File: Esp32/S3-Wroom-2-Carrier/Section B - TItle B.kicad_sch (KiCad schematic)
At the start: 2 parts, among them J1 DF9-21S-1V32, J2 DF9-21S-1V32

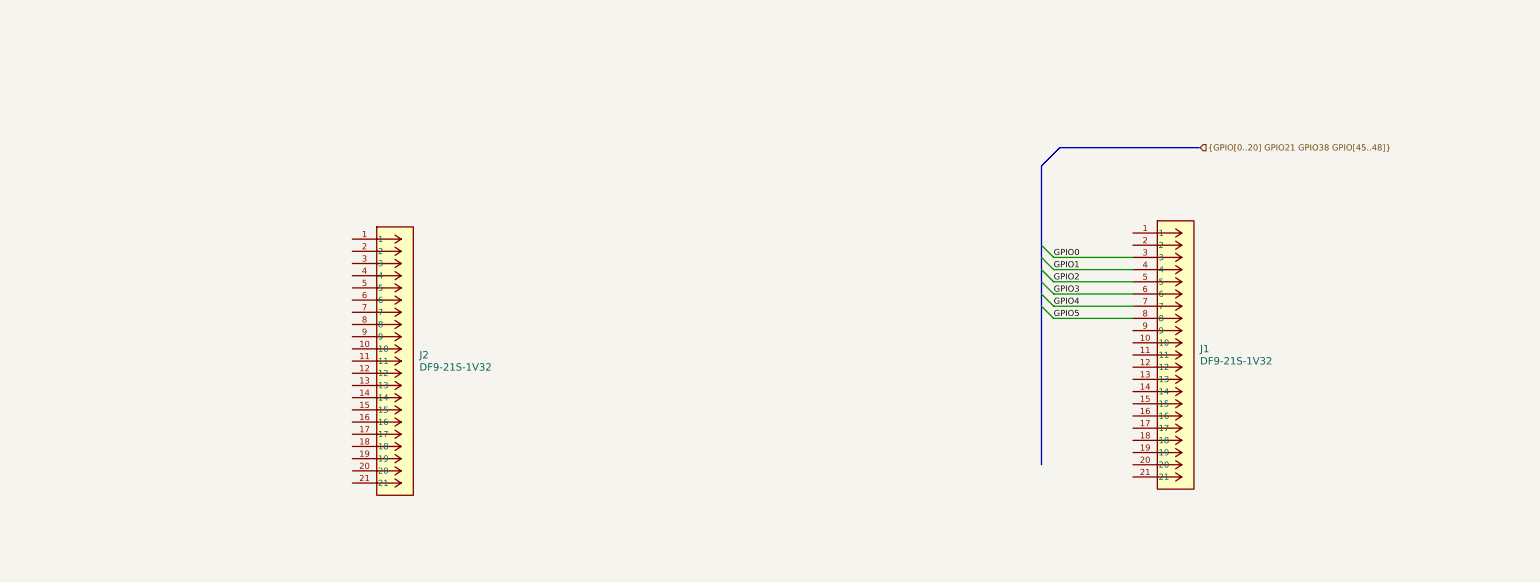
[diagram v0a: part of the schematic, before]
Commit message: Power sheet
Added Esp32 power sheet and rename previous sheets
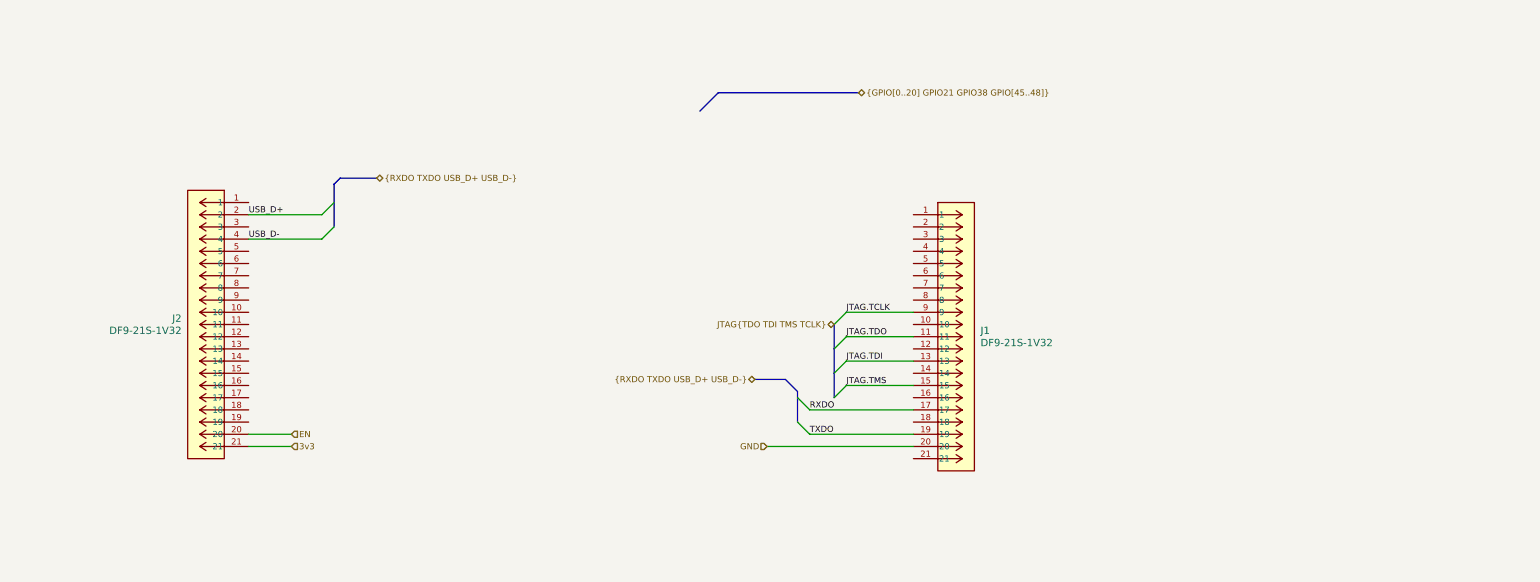
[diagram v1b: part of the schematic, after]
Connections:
- net JTAG.TDO: now reaches J1.11
- net JTAG.TDI: now reaches J1.13
- net JTAG.TMS: now reaches J1.15
- net RXDO: now reaches J1.17
- net TXDO: now reaches J1.19
- net GND: now reaches J1.20
- net JTAG.TCLK: now reaches J1.9
- net USB_D+: now reaches J2.2
- net EN: now reaches J2.20
- net 3v3: now reaches J2.21
- net USB_D-: now reaches J2.4
- net GPIO0: no longer names the net of J1.3
- net GPIO1: no longer names the net of J1.4
- net GPIO2: no longer names the net of J1.5
- net GPIO3: no longer names the net of J1.6
- net GPIO4: no longer names the net of J1.7
- net GPIO5: no longer names the net of J1.8
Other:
- moved on the sheet: J1, J2

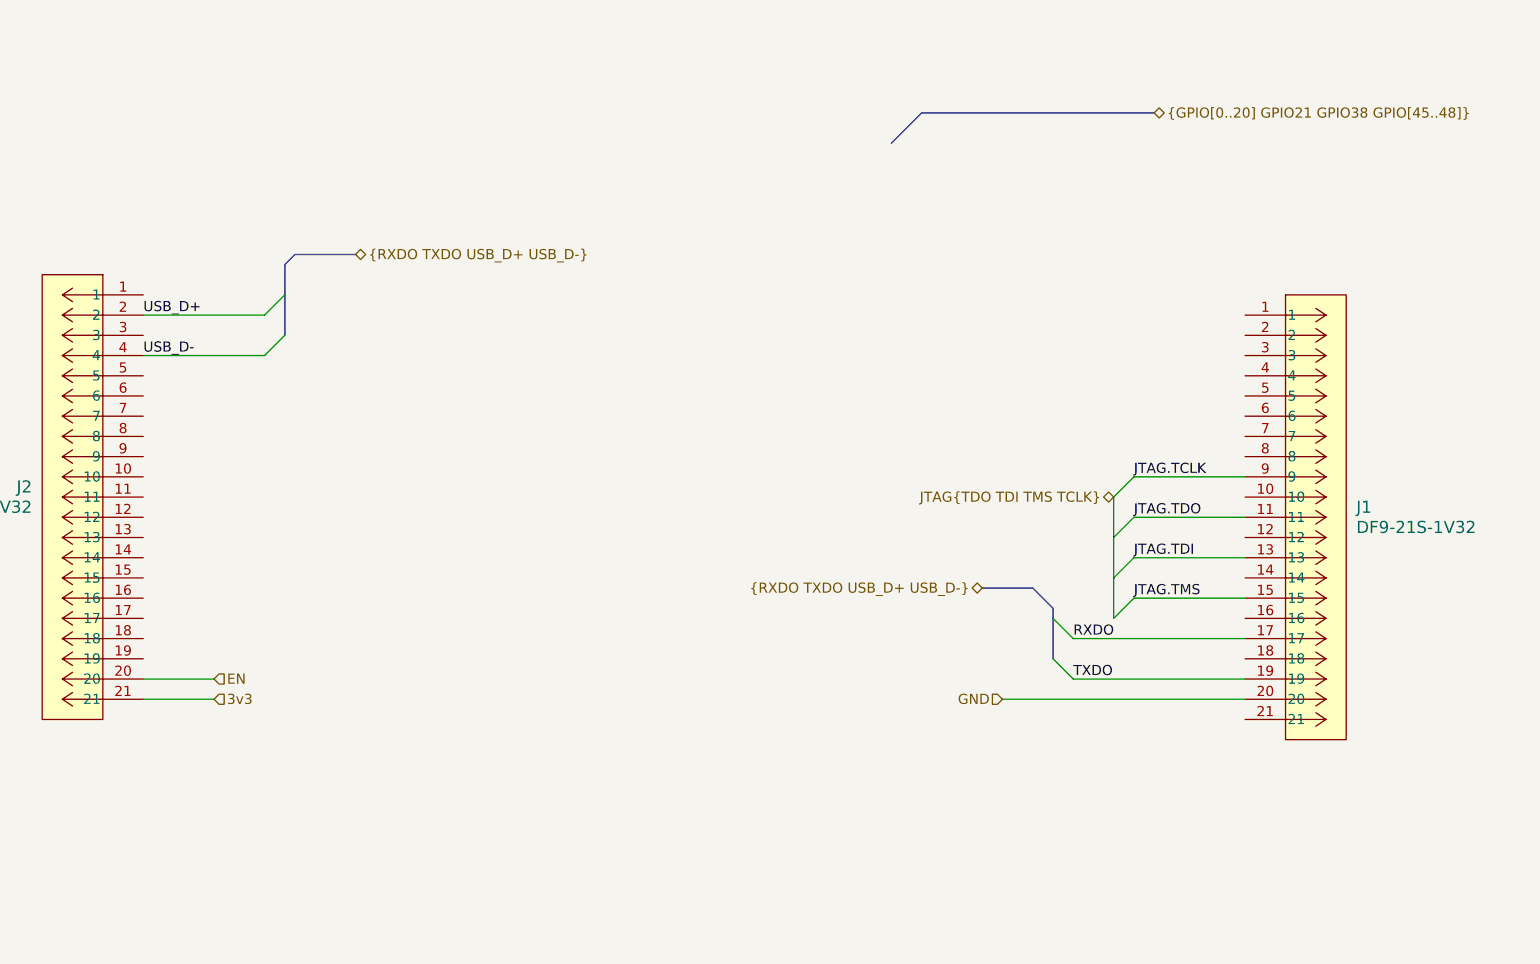
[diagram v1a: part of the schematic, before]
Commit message: Connectors
Lower connector routed
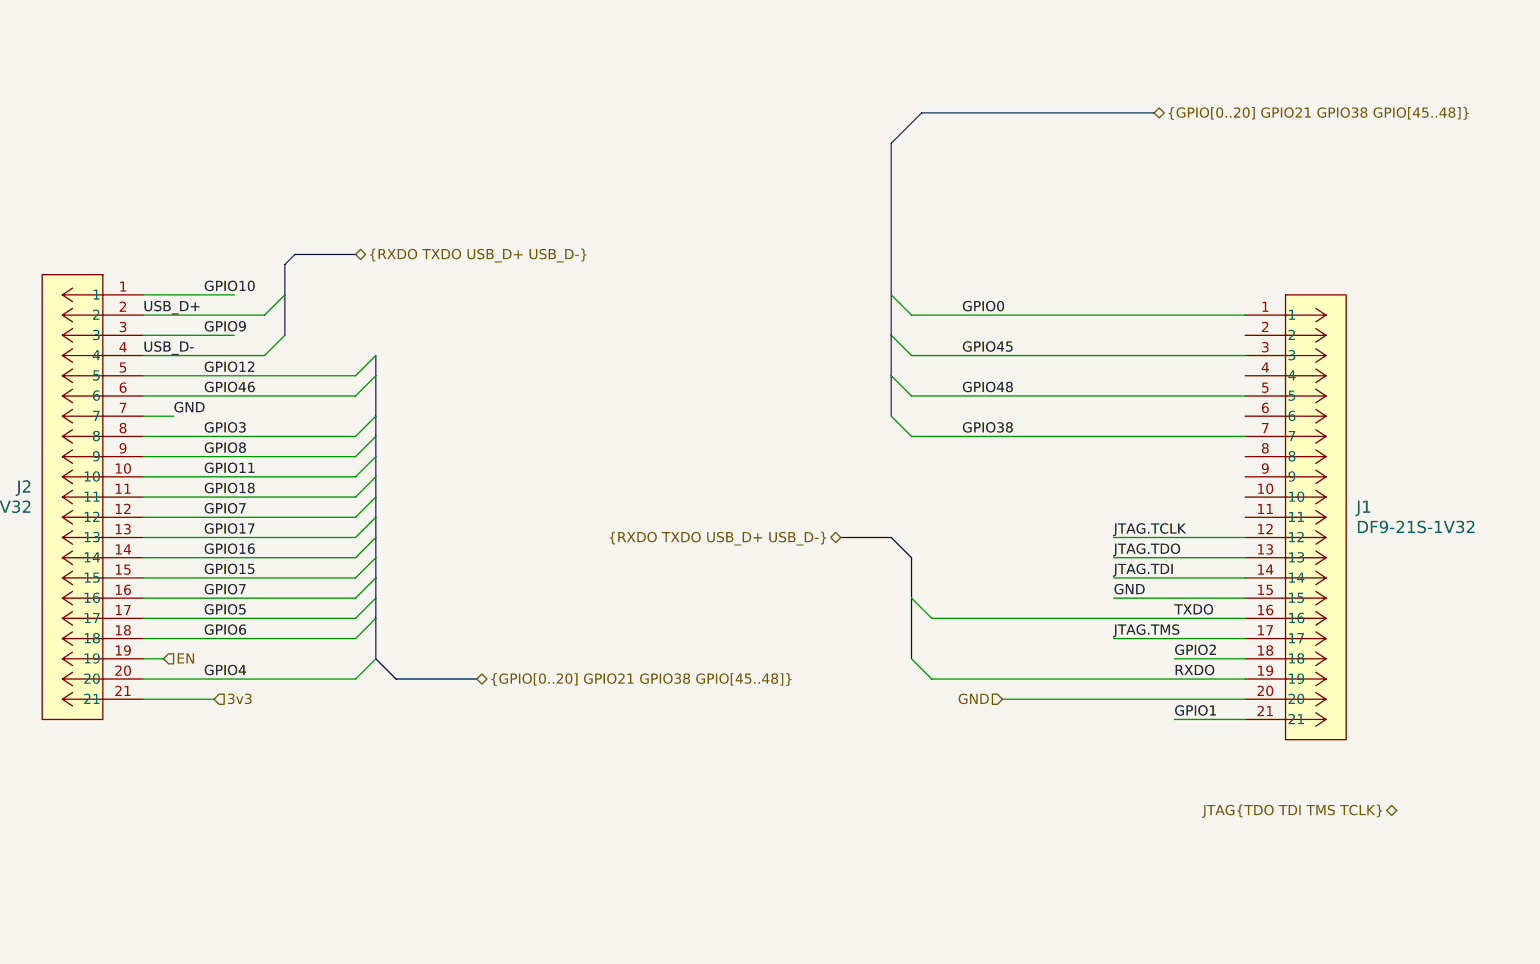
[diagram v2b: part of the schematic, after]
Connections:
- net EN: now also J2.19; no longer J2.20
- net GND: now also J1.15, J2.7
- net JTAG.TCLK: now also J1.12; no longer J1.9
- net JTAG.TDI: now also J1.14; no longer J1.13
- net JTAG.TDO: now also J1.13; no longer J1.11
- net JTAG.TMS: now also J1.17; no longer J1.15
- net RXDO: now also J1.19; no longer J1.17
- net TXDO: now also J1.16; no longer J1.19
- net GPIO0: now reaches J1.1
- net GPIO2: now reaches J1.18
- net GPIO1: now reaches J1.21
- net GPIO45: now reaches J1.3
- net GPIO48: now reaches J1.5
- net GPIO38: now reaches J1.7
- net GPIO10: now reaches J2.1
- net GPIO11: now reaches J2.10
- net GPIO18: now reaches J2.11
- net GPIO7: now reaches J2.12
- net GPIO7: now also J2.16
- net GPIO17: now reaches J2.13
- net GPIO16: now reaches J2.14
- net GPIO15: now reaches J2.15
- net GPIO5: now reaches J2.17
- net GPIO6: now reaches J2.18
- net GPIO9: now reaches J2.3
- net GPIO12: now reaches J2.5
- net GPIO46: now reaches J2.6
- net GPIO3: now reaches J2.8
- net GPIO8: now reaches J2.9
- new net GPIO4: J2.20

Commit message: Routing
Routing finished needs to be verify
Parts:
- removed J1, J2: DF9-21S-1V32, Library:CON9_1X21_DZL_DF9_HIR, symbol Esp32-Carrier-Board:DF9-21S-1V32
- added J4, J5: DF9B-21S-1V69, User_Footprint:CONN_DF9B-21S-1V_21P_HIR, symbol _Connectors:DF9B-21S-1V69
- added R6: 10K, Resistor_SMD:R_0805_2012Metric_Pad1.20x1.40mm_HandSolder, symbol Device:R_US
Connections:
- net 3v3: now also J4.21, R6.1
- net EN: now also J4.19
- net GND: now also J4.12, J4.7, J5.20, J5.9
- net GPIO0: now also J5.1, R6.2
- net GPIO1: now also J5.21
- net GPIO10: now also J4.1
- net GPIO11: now also J4.10
- net GPIO12: now also J4.5
- net GPIO15: now also J4.15
- net GPIO16: now also J4.14
- net GPIO17: now also J4.13
- net GPIO18: now also J4.11
- net GPIO2: now also J5.18
- net GPIO3: now also J4.8
- net GPIO38: now also J5.7
- net GPIO4: now also J4.20
- net GPIO45: now also J5.3
- net GPIO46: now also J4.6
- net GPIO48: now also J5.5
- net GPIO5: now also J4.17
- net GPIO6: now also J4.18
- net GPIO7: now also J4.16
- net GPIO8: now also J4.9
- net GPIO9: now also J4.3
- net JTAG.TCLK: now also J5.13
- net JTAG.TDI: now also J5.15
- net JTAG.TDO: now also J5.14
- net JTAG.TMS: now also J5.17
- net RXDO: now also J5.19
- net TXDO: now also J5.16
- net USB_D+: now also J4.2
- net USB_D-: now also J4.4
- new net GPIO13: J5.6
- new net GPIO14: J5.12
- new net GPIO21: J5.4
- new net GPIO35: J5.2
- new net GPIO36: J5.8
- new net GPIO37: J5.10
- new net GPIO47: J5.11

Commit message: Connectors
change one connector from 21 to 25 pins
Added test points
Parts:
- removed J4: DF9B-21S-1V69, User_Footprint:CONN_DF9B-21S-1V_21P_HIR, symbol _Connectors:DF9B-21S-1V69
- added J1: DF9B-25S-1V32, User_Footprint:CON9_1X25_DL_DF9_HIR, symbol _Connectors:DF9B-25S-1V32
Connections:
- net EN: now also J1.23
- net GND: now also J1.12, J1.17, J1.22, J1.25
- net GPIO10: now also J1.1
- net GPIO11: now also J1.10
- net GPIO12: now also J1.5
- net GPIO15: now also J1.15
- net GPIO16: now also J1.14
- net GPIO17: now also J1.13
- net GPIO18: now also J1.11
- net GPIO3: now also J1.8
- net GPIO4: now also J1.24
- net GPIO46: now also J1.6
- net GPIO5: now also J1.21
- net GPIO6: now also J1.18
- net GPIO7: now also J1.16
- net GPIO8: now also J1.9
- net GPIO9: now also J1.3
- net USB_D+: now also J1.2
- net USB_D-: now also J1.4
- net 3v3 renamed 3V3
- new net PWR_EN: J1.20
- new net VIN: J1.19, J1.7
